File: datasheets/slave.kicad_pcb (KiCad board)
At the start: 2 copper layers, 71.1 x 50.8 mm, 26 parts, among them J1 Screw_Terminal_1x02, J2 Screw_Terminal_1x03, J3 Screw_Terminal_1x02, Q1 IRFU9024N, Q2 IRFU9024N, Q3 IRFU9024N, U1 PC817, U2 PC817, U3 PC817, U4 nRF24L01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

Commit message: Добавил 3D модели
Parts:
- U5: footprint Modules:Arduino_Nano -> arduino:ArduinoNano
- moved U5 19.3 mm to (198.1, 73.7), turned to 0 degrees

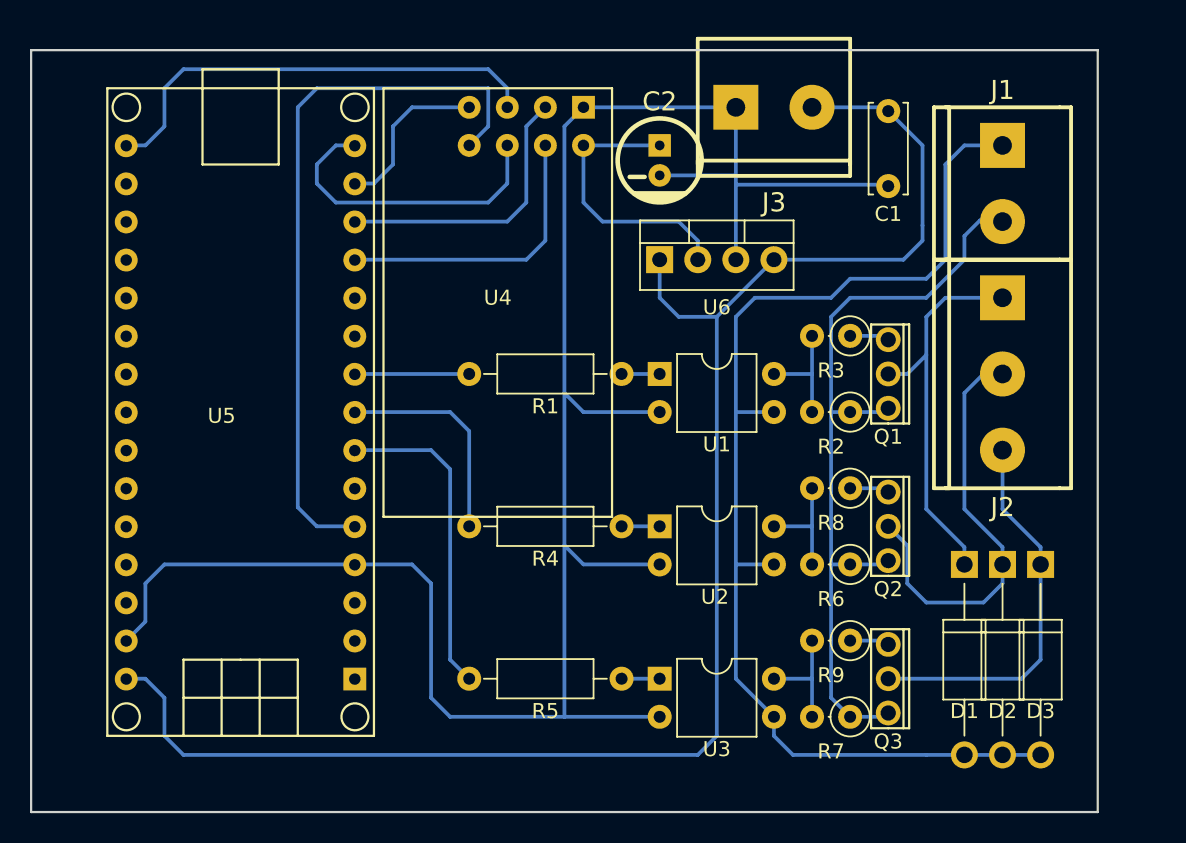
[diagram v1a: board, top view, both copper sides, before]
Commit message: Исправление ошибок. Неправильные MOSI и MISO
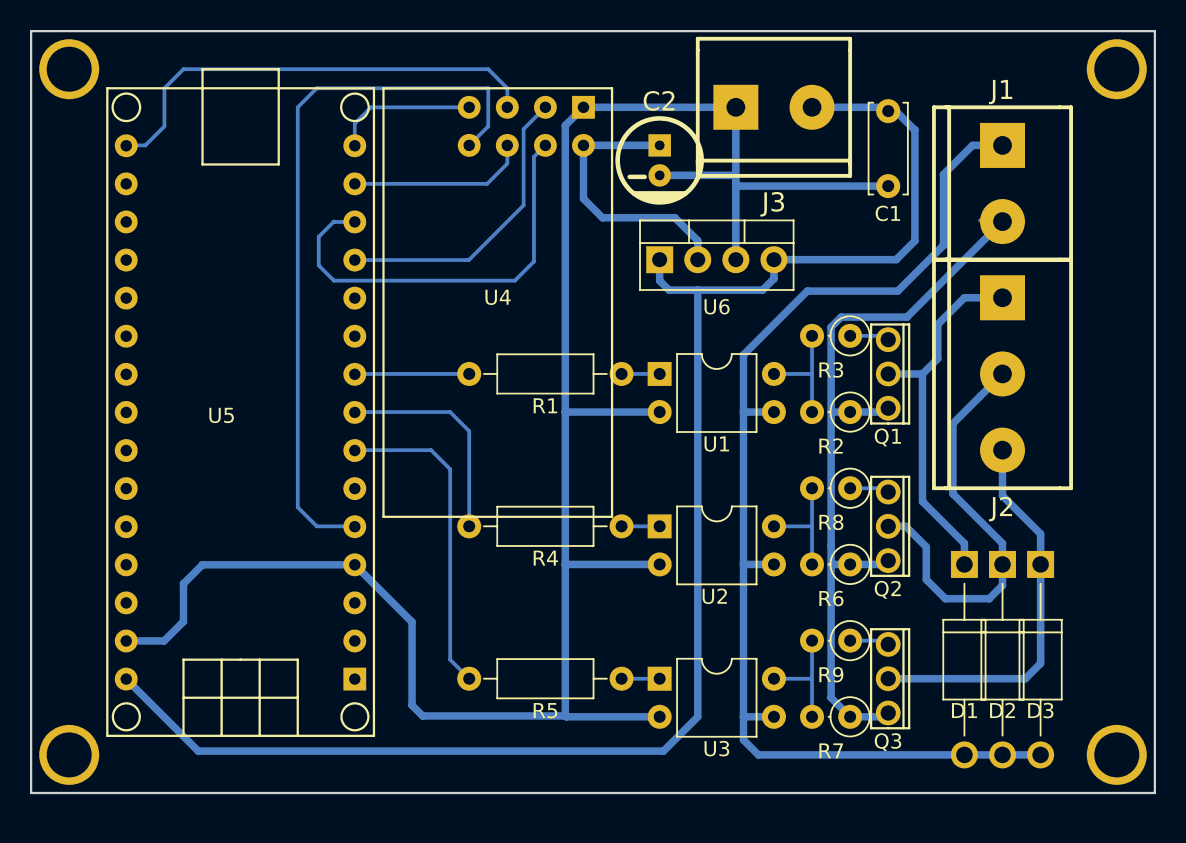
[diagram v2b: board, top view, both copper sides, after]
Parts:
- added REF**: SolderWirePad_single_1-5mmDrill, Wire_Pads:SolderWirePad_single_1-5mmDrill, F.Cu at (186.7, 50.8)
- added REF**: SolderWirePad_single_1-5mmDrill, Wire_Pads:SolderWirePad_single_1-5mmDrill, F.Cu at (186.7, 96.5)
- added REF**: SolderWirePad_single_1-5mmDrill, Wire_Pads:SolderWirePad_single_1-5mmDrill, F.Cu at (256.5, 96.5)
- added REF**: SolderWirePad_single_1-5mmDrill, Wire_Pads:SolderWirePad_single_1-5mmDrill, F.Cu at (256.5, 50.8)
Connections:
- U4 pad 4: /SCN/D9 -> /SCN
- U5 pad 12: /SCN/D9 -> /CE/SS
- U5 pad 13: /CE/SS -> /SCN
- U5 pad 14: /MISO -> /MOSI
- U5 pad 15: /MOSI -> /MISO
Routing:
- net /SCN: track 0.00 -> 28.1 mm
- net /SCN/D9: track 19.6 -> 0.00 mm
- net /MOSI: track 20.6 -> 11.9 mm
- net /D_VCC: track 108.9 -> 104.6 mm
- net /D_GND: track 138.5 -> 136.0 mm
- net /MISO: track 11.2 -> 9.56 mm
- net /OUT_1: track 26.2 -> 24.9 mm
- net /CE/SS: track 18.8 -> 19.9 mm
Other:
- board size 71.1 x 50.8 mm -> 74.9 x 50.8 mm
- net class Power: trace_width 1 -> 0.5

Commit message: Правка схем. Наведение красивости.
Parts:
- moved C1 73.1 mm to (172.7, 79.0)
- moved C2 73.1 mm to (157.5, 82.3)
- moved D3 73.1 mm to (182.9, 109.2)
- moved J3 73.1 mm to (165.1, 78.7)
- moved Q1 73.1 mm to (172.7, 94.2)
- moved Q2 73.1 mm to (172.7, 104.4)
- moved Q3 73.1 mm to (172.7, 114.5)
- moved R1 73.1 mm to (154.9, 96.5)
- moved R4 73.1 mm to (154.9, 106.7)
- moved R5 73.1 mm to (154.9, 116.8)
- moved REF** 73.1 mm to (188.0, 121.9)
- moved REF** 73.1 mm to (188.0, 76.2)
- moved U1 73.1 mm to (157.5, 96.5)
- moved U2 73.1 mm to (157.5, 106.7)
- moved U3 73.1 mm to (157.5, 116.8)
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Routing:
- net /IRQ: track 48.6 -> 38.4 mm
- net /CE/SS: track 19.9 -> 21.5 mm
- net /SCN: track 28.1 -> 28.6 mm
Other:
- board text added: "+12V"
- board text added: "-12V"
- board text added: "BS-slave module rev 1.1 http://alexzulu.ru"
- board text added: "OUT_1"
- board text added: "OUT_2"
- board text added: "OUT_3"
